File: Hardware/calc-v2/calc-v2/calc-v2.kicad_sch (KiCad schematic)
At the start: 74 parts, among them J1 ST-LINK, J2 LCD, SW1 0, SW10 -, SW11 4, SW12 5, SW13 6, SW14 *, SW15 /, SW16 7, SW17 8, SW18 9, SW19 EXP, SW2 /-/, SW20 C, SW21 sqrt, SW22 1/x, SW23 erf, SW24 R->P, SW25 Gamma(x), SW26 Cxy, SW27 y^x, SW28 ln, SW29 log, SW3 ., SW30 sin, SW31 cos, SW32 tan, SW33 Drop, SW34 X<>Y, SW35 DR, SW36 M+, SW37 MR, SW38 MS, SW39 F, SW4 +/-, SW40 G, SW41 Mode, SW42 Uncr, SW43 Prec, SW44 On, SW45 "Reset", SW5 ENTER, SW6 1, SW7 2, SW8 3, SW9 +, U1 TPS61222DCK, U2 STM32L476RETx, Y1 32.768 Hz

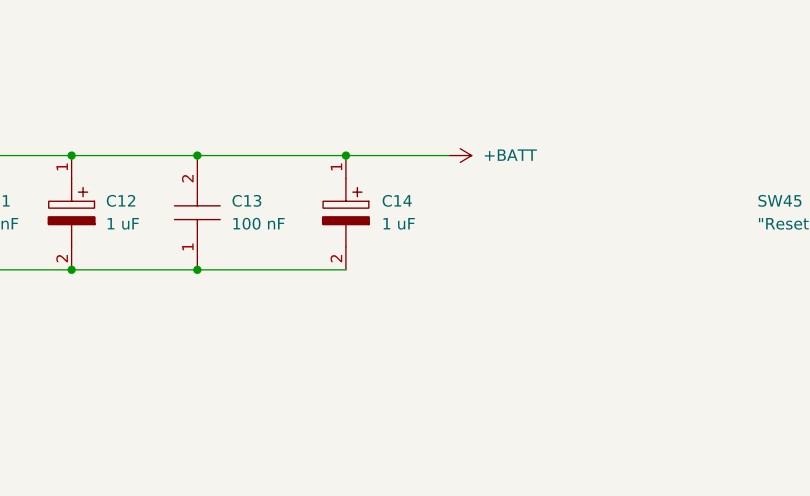
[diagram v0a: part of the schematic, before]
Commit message: Made all footprints handsolder-friendly
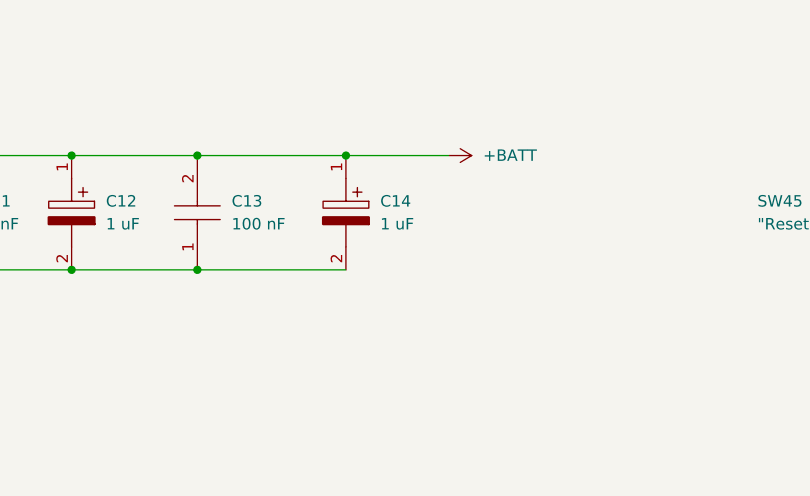
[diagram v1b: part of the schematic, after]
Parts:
- C1, C2: footprint CAPC1608X50N -> C_0603_1608Metric_Pad1.08x0.95mm_HandSolder
- C10, C12, C14: footprint CAPPC1709X100N -> C_0603_1608Metric_Pad1.08x0.95mm_HandSolder
- C11, C13, C3, C4, C5, C6, C8, C9: footprint CAPC1608X90N -> C_0603_1608Metric_Pad1.08x0.95mm_HandSolder
- C15, C7: footprint CAPC1608X87N -> C_0603_1608Metric_Pad1.08x0.95mm_HandSolder
- C16: footprint C0603 -> C_0603_1608Metric_Pad1.08x0.95mm_HandSolder
- D1, D2: footprint Diode_SMD:D_SOD-323 -> D_SOD-323_HandSoldering
- L1, L2, L3: footprint INDC2012X145N -> L_0805_2012Metric_Pad1.15x1.40mm_HandSolder
- R2: footprint RESC1608X55N -> C_0603_1608Metric_Pad1.08x0.95mm_HandSolder

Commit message: Created 3D models for the EVQ switches
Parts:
- BT1: footprint foot-lib:BatteryHolder_Keystone_1057_1x2032 -> foot-lib:BatteryHolder_Keystone_1057
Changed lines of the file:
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@@
       (effects (font (size 1.27 1.27)) (justify left))
     )
-    (property "Footprint" "foot-lib:BatteryHolder_Keystone_1057_1x2032" (id 2) (at 179.07 233.426 90)
+    (property "Footprint" "foot-lib:BatteryHolder_Keystone_1057" (id 2) (at 179.07 233.426 90)
       (effects (font (size 1.27 1.27)) hide)
     )
@@
     )
     (path "/268bb98d-c6ee-4c6a-b5d2-7a103895fb4b"
-      (reference "BT1") (unit 1) (value "3V") (footprint "foot-lib:BatteryHolder_Keystone_1057_1x2032")
+      (reference "BT1") (unit 1) (value "3V") (footprint "foot-lib:BatteryHolder_Keystone_1057")
     )
     (path "/d285528e-510f-4b27-bcfa-93c07bdba5d8"
